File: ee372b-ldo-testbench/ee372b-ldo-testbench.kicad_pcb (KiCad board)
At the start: 4 copper layers, 100 x 100 mm, 129 parts, among them J1 PEC02SAAN, J10 OUT_S, J11 VOUT, J12 VDD_BUF, J13 V_SIG, J14 PEC03SAAN, J15 VSIG_BUF, J16 PEC03SAAN, J17 PEC03SAAN, J18 PEC03SAAN, J19 PEC03SAAN, J2 PEC02SAAN, J20 VREF_EXTERNAL, J21 PEC02SAAN, J22 PEC02SAAN, J23 PEC02SAAN, J24 PEC02SAAN, J25 PEC03SAAN, J3 GND, J4 1V8, J5 3v3_EXTERNAL, J6 GND, J9 IN_S, Q1 FDV305N, Q2 FDV305N, Q3 FDV305N, Q4 FDV305N, Q5 FDV305N, U1 MMSZ4679T1G, U3 ADS1220IPW, U4 BUF634AIDR

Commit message: updated labels, added names
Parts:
- added G***: LOGO, 1_EE372_DemoBoard:Stanford_logo, F.Cu at (164.6, 104.4)
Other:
- board text added: "EE 372B Fall 2026 natagoh l1gong"
- board text added: "VDD_BUF"
- board text added: "VIN 1.8V MAX"

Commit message: fixing PCB
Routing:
- net Net-(U2-OTA_OUT): track 24.5 -> 32.0 mm
- net /VSIG_BUF: track 19.6 -> 14.7 mm
- net Net-(U2-BGR_VREF): track 51.4 -> 55.6 mm
- net Net-(R49-Pad1): track 38.4 -> 39.8 mm
- net /AIN0_SIGNAL: track 27.1 -> 25.9 mm
- net /BGR_VREF: track 31.3 -> 30.7 mm
- net GND: vias 68 -> 67
- net /AIN3_LDO_GND: vias 1 -> 0
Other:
- board text added: "VAR_LOAD_OUT"

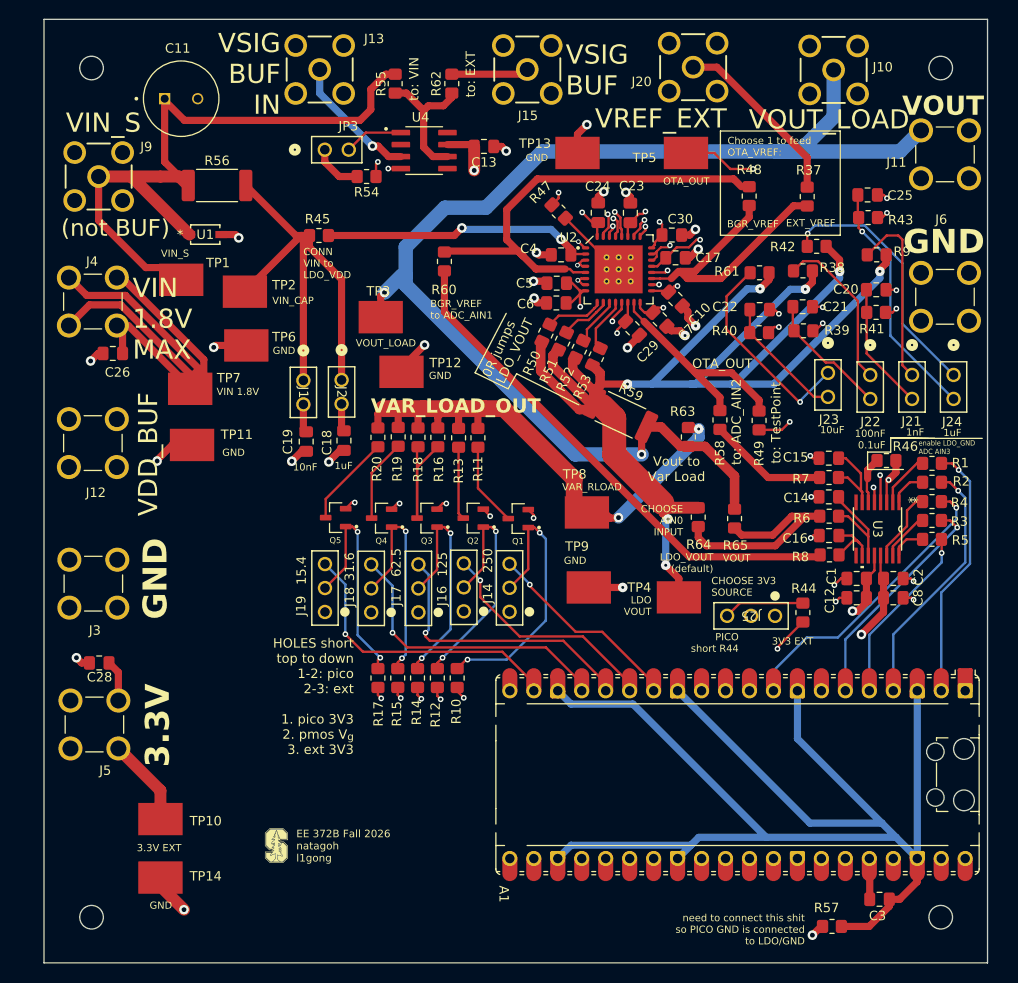
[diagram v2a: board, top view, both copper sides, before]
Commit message: otuput bank traces thicker
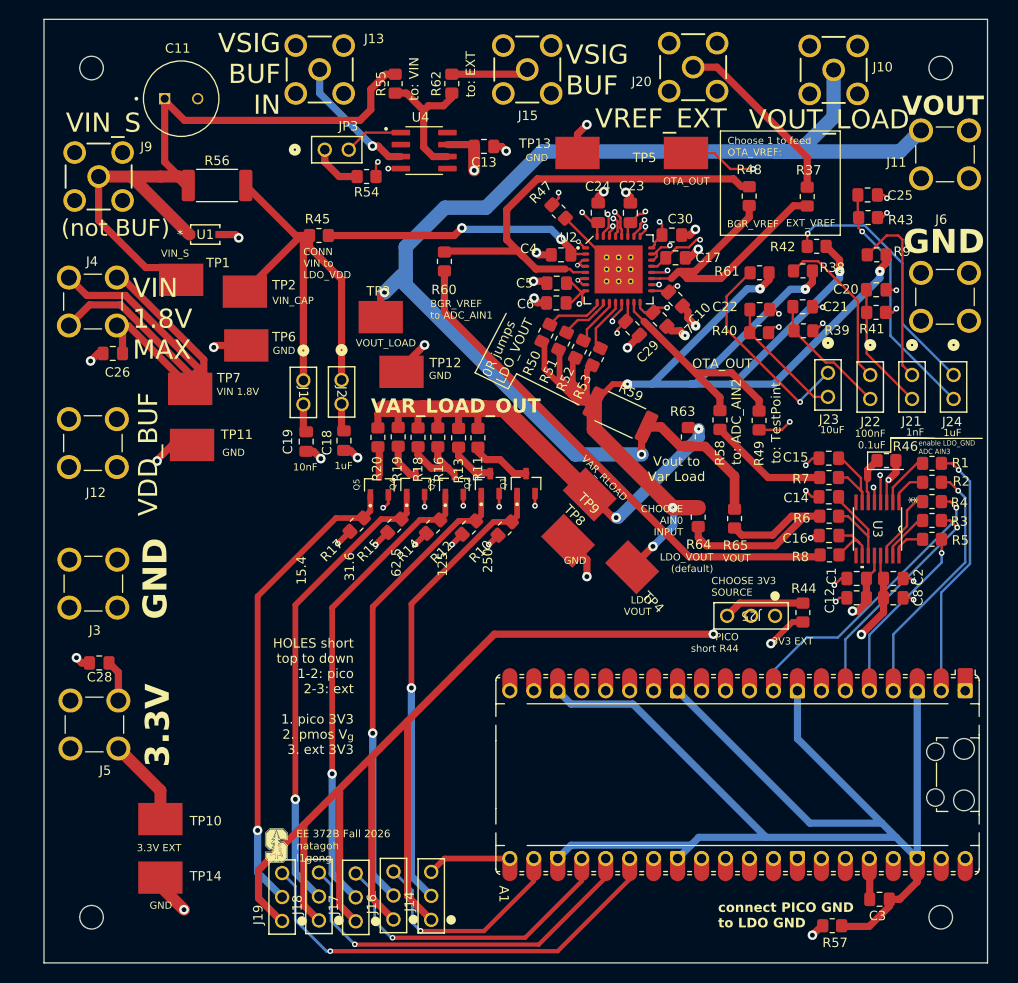
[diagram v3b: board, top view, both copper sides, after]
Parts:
- moved J14 33.7 mm to (181.0, 112.3)
- moved J16 33.5 mm to (177.0, 112.2)
- moved J17 33.4 mm to (173.0, 112.4)
- moved J18 33.1 mm to (169.1, 112.3)
- moved J19 33.1 mm to (165.2, 112.4)
- moved R10 16.6 mm to (188.8, 70.8), turned to -135 degrees
- moved R17 16.4 mm to (173.1, 70.4), turned to -135 degrees
- moved R12 16.3 mm to (185.0, 70.7), turned to -135 degrees
- moved R15 16.1 mm to (177.1, 70.5), turned to -135 degrees
- moved R14 16.1 mm to (181.2, 70.6), turned to -135 degrees
- moved TP4 5.89 mm to (202.3, 74.9), turned to 135 degrees
- moved Q5 5.78 mm to (175.5, 66.2), turned to 90 degrees
- moved TP9 5.42 mm to (195.5, 72.1), turned to 135 degrees
- moved Q4 5.07 mm to (179.3, 66.1), turned to 90 degrees
- moved Q3 4.59 mm to (183.4, 66.1), turned to 90 degrees
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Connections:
- A1 pad 14: /pico_vg0 -> unconnected-(A1-GPIO10-Pad14)_1
- A1 pad 15: /pico_vg1 -> unconnected-(A1-GPIO11-Pad15)_1
- A1 pad 16: /pico_vg2 -> unconnected-(A1-GPIO12-Pad16)
- A1 pad 17: /pico_vg3 -> unconnected-(A1-GPIO13-Pad17)_1
- A1 pad 19: /pico_vg4 -> unconnected-(A1-GPIO14-Pad19)
- A1 pad 21: unconnected-(A1-GPIO16-Pad21)_1 -> /pico_vg0
- A1 pad 22: unconnected-(A1-GPIO17-Pad22) -> /pico_vg1
- A1 pad 24: unconnected-(A1-GPIO18-Pad24) -> /pico_vg2
- A1 pad 25: unconnected-(A1-GPIO19-Pad25)_1 -> /pico_vg3
- A1 pad 26: unconnected-(A1-GPIO20-Pad26)_1 -> /pico_vg4
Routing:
- net /3V3: track 114.2 -> 169.6 mm, vias 2 -> 3
- net /VG4: track 24.5 -> 50.4 mm, vias 2 -> 1
- net /VG3: track 24.0 -> 49.8 mm, vias 2 -> 1
- net /VG2: track 24.8 -> 49.9 mm, vias 2 -> 1
- net /VG1: track 25.9 -> 49.3 mm, vias 2 -> 1
- net /VG0: track 29.7 -> 49.3 mm, vias 2 -> 1
- net /pico_vg4: track 30.5 -> 46.9 mm
- net /pico_vg0: track 20.7 -> 8.92 mm, vias 1 -> 0
- net /pico_vg3: track 30.4 -> 40.0 mm
- net /VD2: track 16.1 -> 8.42 mm
- net /VD4: track 9.80 -> 3.04 mm
- net /VD3: track 8.78 -> 4.09 mm
- net GND: track 125.0 -> 129.5 mm
- net /VARIABLE_LOAD: track 59.0 -> 55.3 mm
- net /pico_vg2: track 29.4 -> 32.6 mm
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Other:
- board text added: "connect PICO GND to LDO GND"
- board text removed: "need to connect this shit so PICO GND is connected to LDO/GND"

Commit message: finished thcicker traces whole board
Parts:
- removed R38, R39, R41, R9: 0, Resistor_SMD:R_0805_2012Metric_Pad1.20x1.40mm_HandSolder
- moved J11 33.3 mm to (203.5, 21.8), turned to 180 degrees
- moved J20 31.2 mm to (235.3, 38.4)
- moved TP5 30.2 mm to (216.9, 59.9)
- moved J6 29.4 mm to (218.8, 22.0), turned to 180 degrees
- moved C25 23.0 mm to (229.0, 58.4)
- moved R42 22.0 mm to (235.8, 57.9)
- moved R40 20.3 mm to (235.7, 53.6)
- moved R61 20.1 mm to (235.7, 46.6)
- moved G*** 20.1 mm to (160.3, 84.8)
- moved U1 16.4 mm to (146.9, 26.8), turned to 45 degrees
- moved J21 16.1 mm to (225.1, 40.0), turned to 0 degrees
- moved R43 14.8 mm to (235.7, 50.0)
- moved J15 14.6 mm to (176.6, 21.8)
- moved C22 14.2 mm to (228.9, 53.1)
- moved J10 13.8 mm to (235.4, 29.4)
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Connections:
- C20 pad 2: GND -> Net-(C20-Pad2)
- C21 pad 2: GND -> Net-(C21-Pad2)
- C22 pad 2: GND -> Net-(C22-Pad2)
- C25 pad 2: GND -> Net-(C25-Pad2)
- J21 pad 1: Net-(J21-Pad1) -> /LDO_VOUT
- J22 pad 1: Net-(J22-Pad1) -> /LDO_VOUT
- J23 pad 1: Net-(J23-Pad1) -> /LDO_VOUT
- J24 pad 1: Net-(J24-Pad1) -> /LDO_VOUT
- R40 pad 2: Net-(C22-Pad1) -> Net-(C22-Pad2)
- R42 pad 1: /LDO_VOUT -> GND
- R42 pad 2: Net-(J24-Pad1) -> Net-(C25-Pad2)
- R43 pad 2: Net-(C25-Pad1) -> Net-(C21-Pad2)
- R61 pad 1: /LDO_VOUT -> GND
- R61 pad 2: Net-(J23-Pad1) -> Net-(C20-Pad2)
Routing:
- net Net-(R49-Pad1): track 39.8 -> 9.39 mm, vias 2 -> 0
- net Net-(J24-Pad1): track 27.5 -> 0.00 mm, vias 1 -> 0
- net Net-(C25-Pad1): track 25.9 -> 2.88 mm, vias 1 -> 0
- net Net-(J23-Pad1): track 22.3 -> 0.00 mm, vias 1 -> 0
- net Net-(J21-Pad1): track 19.5 -> 0.00 mm
- net Net-(J22-Pad1): track 17.4 -> 0.00 mm
- net Net-(U2-OTA_OUT): track 32.0 -> 16.5 mm
- net /VOUT: track 132.0 -> 145.2 mm, vias 2 -> 4
- net Net-(C21-Pad1): track 13.7 -> 2.61 mm
- net Net-(C20-Pad1): track 13.6 -> 2.51 mm
- net Net-(C22-Pad1): track 13.6 -> 2.95 mm
- net Net-(C20-Pad2): track 0.00 -> 6.66 mm
- net Net-(C21-Pad2): track 0.00 -> 5.86 mm
- net /VSIG: track 13.9 -> 18.9 mm
- net Net-(C25-Pad2): track 0.00 -> 4.97 mm
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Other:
- board text added: "1. PICO 3V3 2. PMOS V_{G} 3. EXT 3V3"
- board text added: "100nF ESR"
- board text added: "10uF ESR"
- board text added: "125R"
- board text added: "15.4R"
- board text added: "1nF ESR"
- board text added: "1uF ESR"
- board text added: "250R"
- board text added: "31.6R"
- board text added: "62.5R"
- board text added: "BGR VREF"
- board text added: "EE 372B, Fall 2026 LDO Testbench, Rev2 October 2026 natagoh l1gong"
- board text added: "EXT VREF"
- board text added: "SHUNT to SELECT V_{G} Source 1-2: PICO 3V3 2-3: EXT 3V3"
- board text added: "VOUT LOAD"
- board text added: "VREF EXT"
- board text added: "VSIG BUF_OUT"
- board text added: "expose VSIG_BUF_OUT"
- board text added: "to: TP5"
- board text removed: "125"
- board text removed: "15.4"
- board text removed: "250"
- board text removed: "31.6"
- board text removed: "62.5"
- board text removed: "BGR_VREF"
- board text removed: "EE 372B Fall 2026 natagoh l1gong"
- board text removed: "EXT_VREF"
- board text removed: "HOLES short top to down 1-2: pico 2-3: ext 1. pico 3V3 2. pmos V_{g} 3. ext 3V3"
- board text removed: "VREF_EXT"
- board text removed: "VSIG BUF"
- board text removed: "to: EXT"
- board text removed: "to: TestPoint"

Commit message: DRC clean
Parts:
- moved TP13 28.9 mm to (217.1, 51.3), turned to 45 degrees
- moved G*** 4.81 mm to (160.6, 89.6)
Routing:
- net /pico_spi_cs: track 27.3 -> 28.0 mm
- removed copper zone on In2.Cu, net /1V8
- removed copper zone on In2.Cu, net /VSIG
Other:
- board text added: "VG0 Q1 J14 250"
- board text added: "VG1 Q2 J16 125"
- board text added: "VG2 Q3 J17 62.5"
- board text added: "VG3 Q4 J18 31.6"
- board text added: "VG4 Q5 J19 15.4"

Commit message: emailed to TAs
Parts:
- moved R62 8.95 mm to (191.3, 25.8), turned to 45 degrees
- moved TP1 6.45 mm to (153.5, 42.5), turned to 135 degrees
- moved TP8 3.58 mm to (196.2, 70.4)
- moved TP9 2.56 mm to (193.5, 73.7)
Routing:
- net /VOUT: track 145.2 -> 161.6 mm, vias 4 -> 5
- net Net-(J15-Pad1): track 6.69 -> 16.8 mm
- net /VARIABLE_LOAD: track 55.3 -> 64.5 mm
- net /VSIG_BUF: track 18.2 -> 25.8 mm
- net /c1_vin_jump: track 50.6 -> 57.8 mm, vias 0 -> 1
- net /LDO_VOUT: track 152.9 -> 158.7 mm, vias 3 -> 4
- net /AIN1_SIGNAL: track 55.0 -> 57.9 mm
- net /1V8: track 70.3 -> 72.0 mm, vias 0 -> 1
- net GND: track 126.4 -> 125.8 mm, vias 63 -> 72
- net /3V3_PICO: vias 1 -> 4
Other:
- board text added: "Kelvin Tap Measure I_IN"
- board text added: "Kelvin Tap Measure I_OUT"
- board text added: "Kelvin Tap Measure I_{in}"
- board text added: "SPI IRQ"
- board text added: "SPI_CLK"
- board text added: "SPI_CS"
- board text added: "SPI_RX"
- board text added: "SPI_TX"
- board text added: "VREF_EXT"
- board text removed: "VAR_RLOAD"
- board text removed: "VOUT LOAD"
- board text removed: "VREF EXT"

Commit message: forgot drill files last time
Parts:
- added TP14: TestPoint_Probe, TestPoint:TestPoint_Pad_D1.0mm, F.Cu at (158.1, 43.2)
- added TP15: GND, 1_EE372_DemoBoard:KEYSTONE_5016, F.Cu at (227.4, 24.2)
- added TP17: TestPoint_Probe, TestPoint:TestPoint_Pad_D1.0mm, F.Cu at (160.3, 42.9)
- added TP18: TestPoint_Probe, TestPoint:TestPoint_Pad_D1.0mm, F.Cu at (199.3, 64.5)
- added TP19: TestPoint_Probe, TestPoint:TestPoint_Pad_D1.0mm, F.Cu at (201.4, 65.2)
- moved TP2 2.76 mm to (164.0, 45.9), turned to 90 degrees
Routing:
- net GND: track 125.8 -> 129.1 mm, vias 72 -> 64
- net /1V8: track 72.0 -> 74.7 mm
- net /VOUT: track 161.6 -> 163.2 mm
- net /c1_vin_jump: track 57.8 -> 59.4 mm
- net /LDO_VOUT: track 158.7 -> 159.3 mm
- net /3V3_PICO: vias 4 -> 1
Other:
- board text added: "EE 372B, October 2026 LDO Testbench, Rev2.2 natagoh l1gong"
- board text added: "EXT VREF OUT"
- board text added: "VREF_EXT INPUT"
- board text removed: "EE 372B, Fall 2026 LDO Testbench, Rev2 October 2026 natagoh l1gong"
- board text removed: "VREF_EXT"
